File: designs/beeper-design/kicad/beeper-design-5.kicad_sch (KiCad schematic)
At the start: 2 parts, among them U2 AT25FF321A-UUN-T

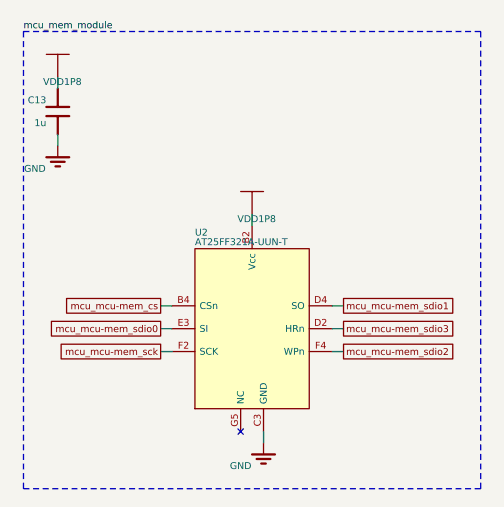
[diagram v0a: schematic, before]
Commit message: fixing drc errors
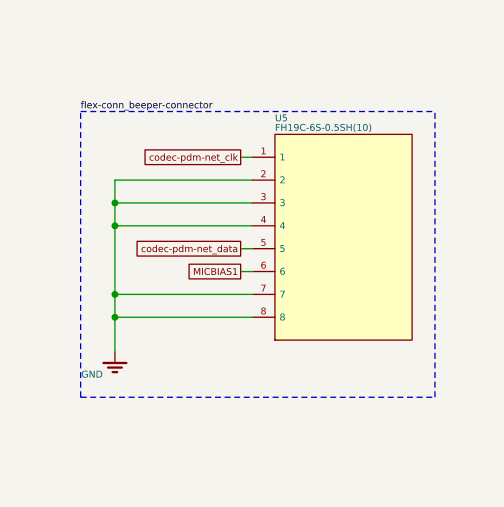
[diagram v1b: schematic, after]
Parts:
- removed C13: 1u, beeper-design:Pkg0201_10, symbol C76935_3
- removed U2: AT25FF321A-UUN-T, beeper-design:WLCSP_12, symbol AT25FF321A_UUN_T
- added U5: FH19C-6S-0.5SH(10), beeper-design:LP_4, symbol FH19C_6S_0_5SH_10_
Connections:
- net GND: now also U5.2, U5.3, U5.4, U5.7, U5.8
- new net MICBIAS1: U5.6
- new net codec-pdm-net_clk: U5.1
- new net codec-pdm-net_data: U5.5

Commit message: another export
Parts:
- removed U5: FH19C-6S-0.5SH(10), beeper-design:LP_4, symbol FH19C_6S_0_5SH_10_
- added C47: 2.2u, beeper-design:Pkg0201_11, symbol C335106_9
- added C48: 2.2u, beeper-design:Pkg0201_24, symbol C335106_17
- added R16, R17: 8K2, beeper-design:Pkg0201_39, symbol my_resistor_9
- added TP1, TP2: (no value), beeper-design:SMD_TESTPT, symbol smd_testpoint_cmp
- added U12: DRV2605YZFR, beeper-design:LP_7, symbol DRV2605YZFR
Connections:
- net GND: now also C47.1, C48.1, U12.B3 (GND)
- new net: C47.2, U12.A2 (REG)
- new net: TP1.p, U12.A3 (OUT+)
- new net: TP2.p, U12.C3 (OUT-)
- new net VDDSYS: C48.2, R16.2, R17.2, U12.C2 (VDD)
- new net mcu_hap-gpio0_gpio: U12.A1 (EN)
- new net mcu_hap-gpio1_gpio: U12.B1 (IN_TRIG)
- new net mcu_hap-i2c_scl: R17.1, U12.C1 (SCL)
- new net mcu_hap-i2c_sda: R16.1, U12.B2 (SDA)
